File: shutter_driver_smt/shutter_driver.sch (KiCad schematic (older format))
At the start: 43 parts, among them J1 SHUTTER, J2 POWER, J3 I/O, J4 FRONT, Q1 2N3904, Q2 FQP30N06L-ND, Q3 2N3904, Q4 2N3904, Q5 Q_PMOS_GDS, SW1 SW_DPDT_x2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

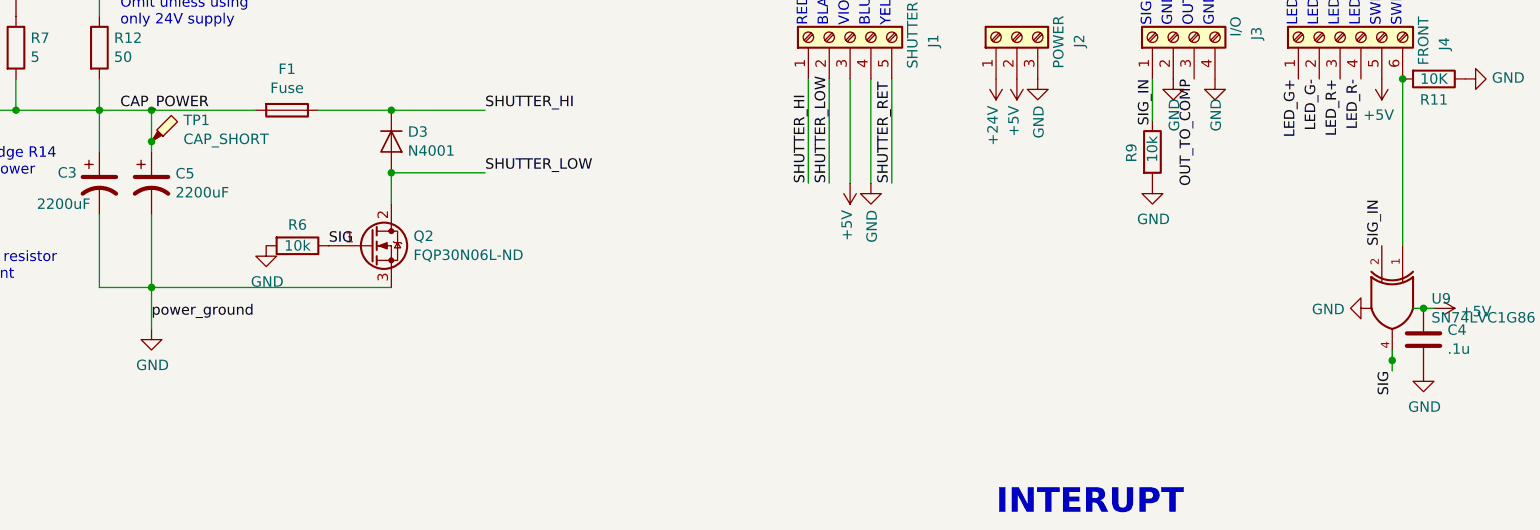
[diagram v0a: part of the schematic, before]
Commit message: added bypass for gate
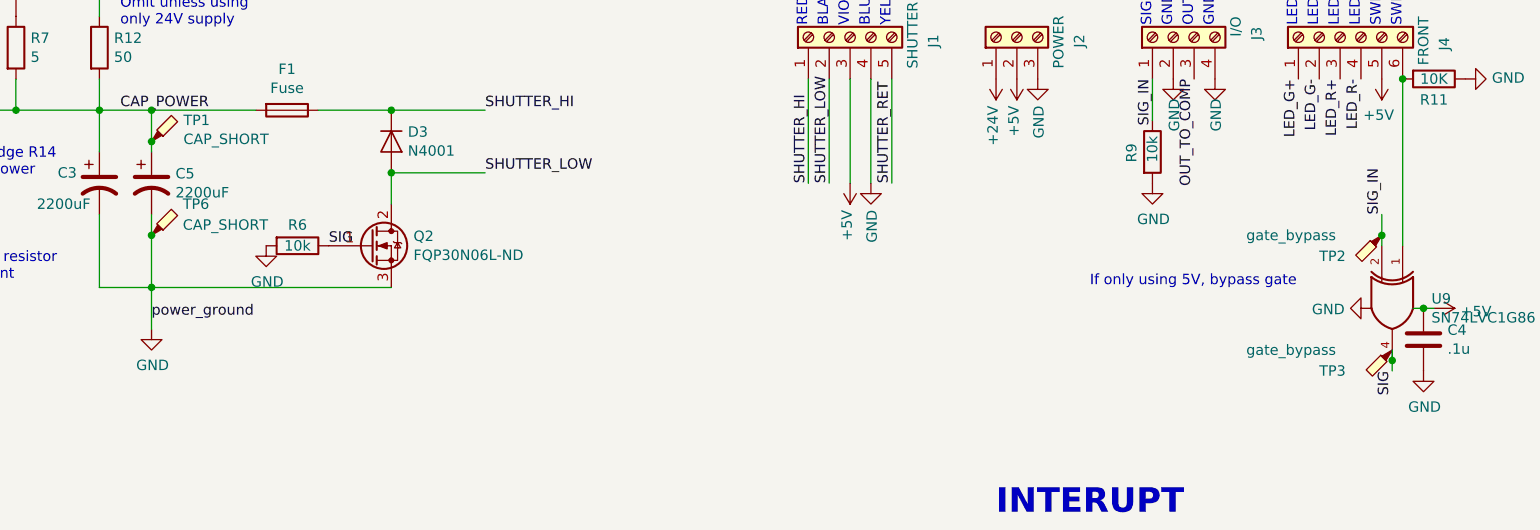
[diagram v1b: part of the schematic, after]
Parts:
- added TP2, TP3: gate_bypass, Connector_Wire:SolderWirePad_1x01_Drill1.2mm, symbol Connector:TestPoint_Probe
- added TP6: CAP_SHORT, Measurement_Points:Measurement_Point_Round-SMD-Pad_Small, symbol Connector:TestPoint_Probe
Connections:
- net GND: now also TP6.1
- net SIG: now also TP3.1
- net SIG_IN: now also TP2.1
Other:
- note added: "If only using 5V, bypass gate"
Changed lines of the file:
@@
 	0    1    1    0
 $EndComp
-Text Label 10200 2600 1    50   ~ 0
+Text Label 10200 2450 1    50   ~ 0
 SIG_IN
 $Comp
@@
 	10400 2900 10450 2900
 Wire Wire Line
-	4300 2450 4300 2800
+	4300 2450 4300 2550
 Wire Wire Line
 	4300 2800 4300 3000
@@
 $EndComp
 Connection ~ 8850 4750
+Wire Wire Line
+	10200 2600 10200 2550
+$Comp
+L Connector:TestPoint_Probe TP2
+U 1 1 5CE6E424
+P 10200 2550
+F 0 "TP2" H 10500 2650 50  0000 R CNN
+F 1 "gate_bypass" H 10850 2550 50  0000 R CNN
+F 2 "Connector_Wire:SolderWirePad_1x01_Drill1.2mm" H 10400 2550 50  0001 C CNN
+F 3 "~" H 10400 2550 50  0001 C CNN
+	1    10200 2550
+	-1   0    0    1
+$EndComp
+Wire Wire Line
+	10200 2550 10200 2450
+Connection ~ 10200 2550
+$Comp
+L Connector:TestPoint_Probe TP3
+U 1 1 5CE6E50A
+P 10250 3100
+F 0 "TP3" H 10600 3200 50  0000 R CNN
+F 1 "gate_bypass" H 10950 3100 50  0000 R CNN
+F 2 "Connector_Wire:SolderWirePad_1x01_Drill1.2mm" H 10450 3100 50  0001 C CNN
+F 3 "~" H 10450 3100 50  0001 C CNN
+	1    10250 3100
+	-1   0    0    1
+$EndComp
+Text Notes 8800 2800 0    50   ~ 0
+If only using 5V, bypass gate
+$Comp
+L Connector:TestPoint_Probe TP6
+U 1 1 5CE73A6C
+P 4300 2550
+F 0 "TP6" H 4450 2700 50  0000 L CNN
+F 1 "CAP_SHORT" H 4450 2600 50  0000 L CNN
+F 2 "Measurement_Points:Measurement_Point_Round-SMD-Pad_Small" H 4500 2550 50  0001 C CNN
+F 3 "~" H 4500 2550 50  0001 C CNN
+	1    4300 2550
+	1    0    0    -1
+$EndComp
+Connection ~ 4300 2550
+Wire Wire Line
+	4300 2550 4300 2800
 $EndSCHEMATC
